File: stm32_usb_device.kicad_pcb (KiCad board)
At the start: 4 copper layers, 45.5 x 16 mm, 33 parts, among them J1 Conn_01x04, J2 Conn_01x04, J3 Conn_01x04, J4 USB_A, J5 Conn_01x05, U1 HT7533-1, U2 SRV05-4, U3 STM32F103C8T6, Y1 16M

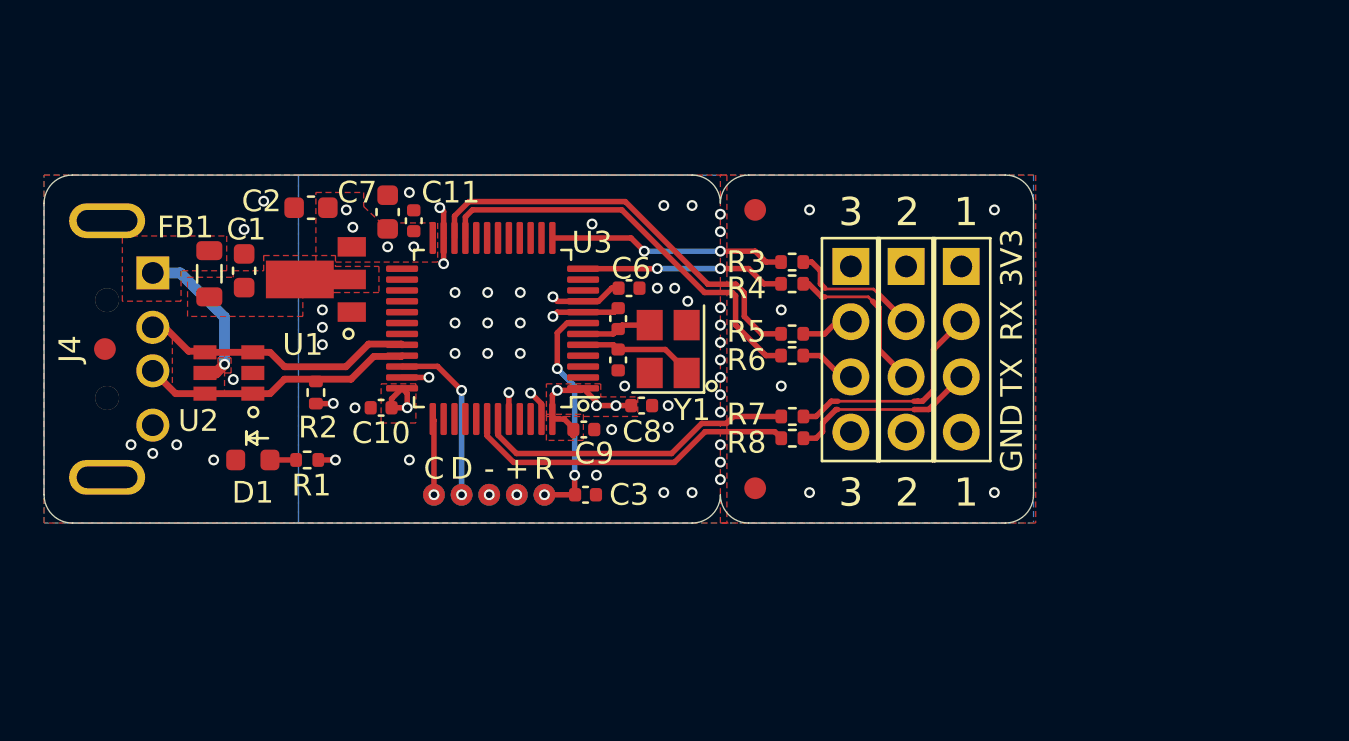
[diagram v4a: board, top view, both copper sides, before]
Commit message: Update project to KiCad v6
Signed-off-by: Tomislav Milkovic <tomislav.milkovic95@gmail.com>
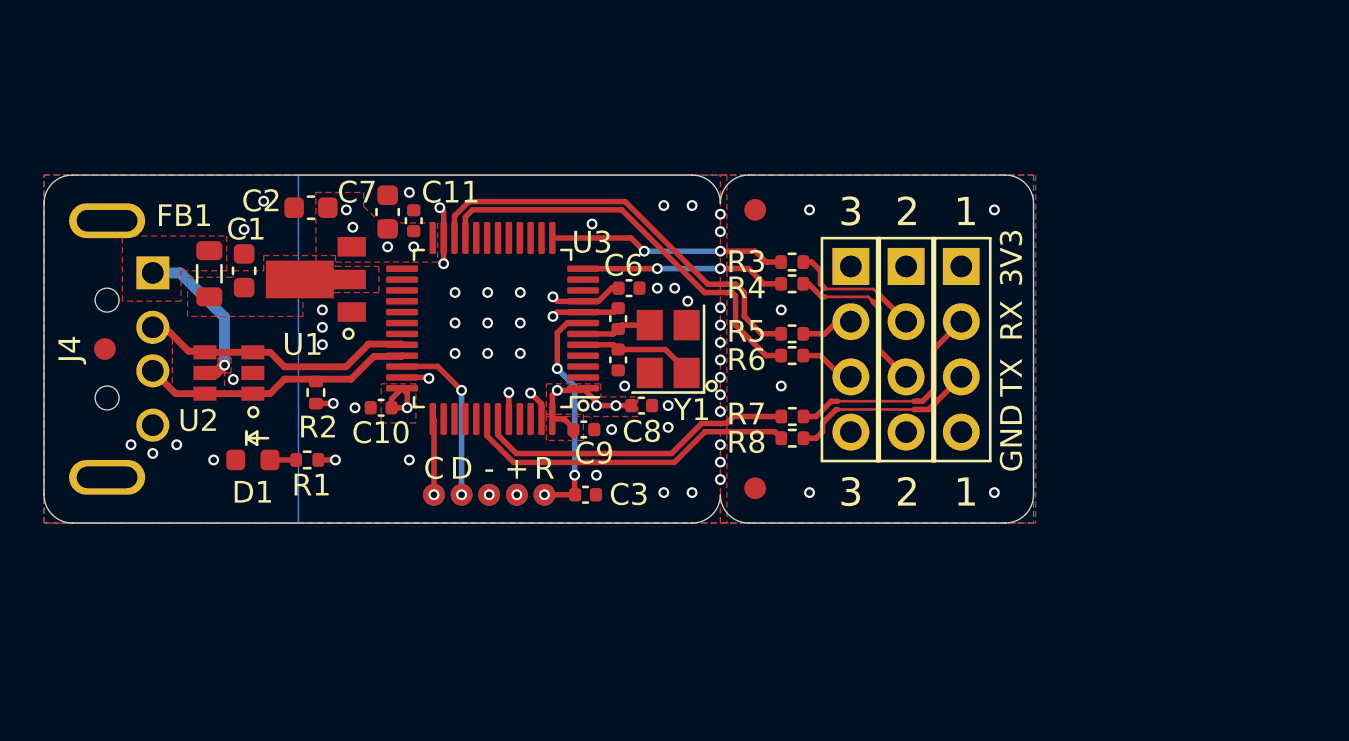
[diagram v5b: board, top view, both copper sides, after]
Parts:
- turned FB1 to -90 degrees
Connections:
- net +3V3 renamed +3.3V
- net /~RESET renamed /~{RESET}
- FB1 pad 1: /5V_FLT -> +5V
- FB1 pad 2: +5V -> /5V_FLT
- J4 pad 5: Net-(J4-Pad5) -> unconnected-(J4-Pad5)
- U3 pad 10: (no net) -> unconnected-(U3-Pad10)
- U3 pad 11: (no net) -> unconnected-(U3-Pad11)
- U3 pad 14: (no net) -> unconnected-(U3-Pad14)
- U3 pad 15: (no net) -> unconnected-(U3-Pad15)
- U3 pad 16: (no net) -> unconnected-(U3-Pad16)
- U3 pad 17: (no net) -> unconnected-(U3-Pad17)
- U3 pad 18: (no net) -> unconnected-(U3-Pad18)
- U3 pad 19: (no net) -> unconnected-(U3-Pad19)
- U3 pad 2: (no net) -> unconnected-(U3-Pad2)
- U3 pad 20: (no net) -> unconnected-(U3-Pad20)
- U3 pad 25: (no net) -> unconnected-(U3-Pad25)
- U3 pad 26: (no net) -> unconnected-(U3-Pad26)
- U3 pad 27: (no net) -> unconnected-(U3-Pad27)
- U3 pad 28: (no net) -> unconnected-(U3-Pad28)
- U3 pad 29: (no net) -> unconnected-(U3-Pad29)
- U3 pad 3: (no net) -> unconnected-(U3-Pad3)
- U3 pad 30: (no net) -> unconnected-(U3-Pad30)
- U3 pad 31: (no net) -> unconnected-(U3-Pad31)
- U3 pad 38: (no net) -> unconnected-(U3-Pad38)
- U3 pad 39: (no net) -> unconnected-(U3-Pad39)
- U3 pad 4: (no net) -> unconnected-(U3-Pad4)
- U3 pad 40: (no net) -> unconnected-(U3-Pad40)
- U3 pad 41: (no net) -> unconnected-(U3-Pad41)
- U3 pad 45: (no net) -> unconnected-(U3-Pad45)
- U3 pad 46: (no net) -> unconnected-(U3-Pad46)
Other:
- net class Default removed
- net class USB removed
